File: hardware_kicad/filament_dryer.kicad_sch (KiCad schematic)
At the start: 60 parts, among them J1 grove_vert_holes, J2 USB_C_Receptacle_USB2.0, J3 grove_vert_holes, Q1 NMOS, U1 W25Q128JVS, U2 AMS1117-3.3, U3 RP2040, U4 DS18B20Z, U5 SHT31-DIS, U6 DS18B20Z, X1 12MHz Yangxing Tech X322512MS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

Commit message: Added new parts
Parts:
- removed R11: 10k, Resistor_SMD:R_0402_1005Metric_Pad0.72x0.64mm_HandSolder, symbol 00_project_library:R
- removed TP7: TestPoint, TestPoint:TestPoint_Pad_D1.0mm, symbol Connector:TestPoint
- added C14: 10u, Capacitor_SMD:C_0603_1608Metric, symbol 00_project_library:C
- added HT_FILAMENT_SCL: TestPoint, TestPoint:TestPoint_Pad_D1.5mm, symbol Connector:TestPoint
- added R17, R18: 10k, Resistor_SMD:R_0402_1005Metric_Pad0.72x0.64mm_HandSolder, symbol 00_project_library:R
- added TP6: HT_FILAMENT_SCA, TestPoint:TestPoint_Pad_D1.5mm, symbol Connector:TestPoint
- TP2: value TestPoint -> HT_FILAMENT_GND
- TP3: value TestPoint -> HT_FILAMENT_3V3
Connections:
- net +3V3: now also TP3.1, C14.1, R17.1, R18.1
- net GND: now also TP2.1, U5.2 (ADDR), C14.2
- net HUMIDITY_GROVE_SCL: no longer J1.1
- net HUMIDITY_GROVE_SDA: no longer J1.2
- net HUMIDITY_SCL: no longer R14.2, TP3.1, U5.4 (SCL)
- net HUMIDITY_SDA: no longer R13.2, TP2.1, U5.1 (SDA)
- net TEMP_BOARD_1WIRE: no longer R15.2, TP4.1, U4.4 (DQ)
- net TEMP_GROVE_1WIRE: no longer J3.1, R16.2
- net TEMP_HEATING_1WIRE: no longer R1.2, TP5.1, U6.4 (DQ)
- new net HT_FILAMENT_SCL: HT_FILAMENT_SCL.1, R18.2
- new net HT_FILAMENT_SDA: R17.2, TP6.1
- new net HT_GROVE_SCL: J1.1
- new net HT_GROVE_SDA: J1.2
- new net HT_SILICAGEL_SCL: R14.2, U5.4 (SCL)
- new net HT_SILICAGEL_SDA: R13.2, U5.1 (SDA)
- new net T_BOARD_1WIRE: R15.2, TP4.1, U4.4 (DQ)
- new net T_GROVE_1WIRE: J3.1, R16.2
- new net T_HEATING_1WIRE: R1.2, TP5.1, U6.4 (DQ)
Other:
- note added: "H/T Ambient"
- note added: "H/T Filament"
- note added: "H/T Silicagel"
- note removed: "Humidity"
- moved on the sheet: C13, C15, C20, D2, J1, JP1, Q1, R10, R12, R13, R14, R7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

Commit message: Some more layout
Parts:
- removed JP1: Jumper_2_Bridged, Jumper:SolderJumper-2_P1.3mm_Open_RoundedPad1.0x1.5mm, symbol Jumper:Jumper_2_Bridged
- added D1: HEATER_2, LED_SMD:LED_0603_1608Metric, symbol 00_project_library:LED
- added D4, D5: 1N4148WS, Diode_SMD:D_SOD-323, symbol Diode:1N4148WS
- added D6: FAN_1, LED_SMD:LED_0603_1608Metric, symbol 00_project_library:LED
- added D7: FAN_2, LED_SMD:LED_0603_1608Metric, symbol 00_project_library:LED
- added H5: MountingHole, MountingHole:MountingHole_3.2mm_M3, symbol 00_project_library:MountingHole
- added J4: Peristatic Pump, 00_project_library:grove_vert_holes, symbol 00_project_library:grove_vert_holes
- added Q2, Q3, Q4: NMOS, Package_TO_SOT_SMD:SOT-23, symbol 00_project_library:NMOS
- added R11, R19, R20, R22: 470R, Resistor_SMD:R_0402_1005Metric_Pad0.72x0.64mm_HandSolder, symbol 00_project_library:R
- added R_POWER1_10, R_POWER1_11, R_POWER1_12, R_POWER1_2, R_POWER1_3, R_POWER1_4, R_POWER1_5, R_POWER1_6, R_POWER1_7, R_POWER1_8, R_POWER1_9, R_POWER2_1, R_POWER2_10, R_POWER2_11, R_POWER2_12, R_POWER2_2, R_POWER2_3, R_POWER2_4, R_POWER2_5, R_POWER2_6, R_POWER2_7, R_POWER2_8, R_POWER2_9: 120, Resistor_SMD:R_1206_3216Metric, symbol 00_project_library:R_POWER
- added TP10: FAN_SILICAGEL_BLACK, TestPoint:TestPoint_Pad_D3.0mm, symbol Connector:TestPoint
- added TP7: FAN_AMBIENT_RED, TestPoint:TestPoint_Pad_D3.0mm, symbol Connector:TestPoint
- added TP8: FAN_AMBIENT_BLACK, TestPoint:TestPoint_Pad_D3.0mm, symbol Connector:TestPoint
- added TP9: FAN_SILICAGEL_RED, TestPoint:TestPoint_Pad_D3.0mm, symbol Connector:TestPoint
- D2: value HEATING_LED -> HEATER_1
- H1, H2, H3, H4: footprint MountingHole:MountingHole_2.2mm_M2 -> MountingHole:MountingHole_3.2mm_M3
- J2: renamed from J1; value grove_vert_holes -> H/T Ambient
- J3: value grove_vert_holes -> T Aux
- TP11: renamed from HT_FILAMENT_SCL; value TestPoint -> HT_SILICAGEL_SCL; footprint TestPoint:TestPoint_Pad_D1.5mm -> TestPoint:TestPoint_Pad_D3.0mm
- TP2: value HT_FILAMENT_GND -> HT_SILICAGEL_GND; footprint TestPoint:TestPoint_Pad_D1.5mm -> TestPoint:TestPoint_Pad_D3.0mm
- TP3: value HT_FILAMENT_3V3 -> HT_SILICAGEL_3V3; footprint TestPoint:TestPoint_Pad_D1.5mm -> TestPoint:TestPoint_Pad_D3.0mm
- TP4, TP5: footprint TestPoint:TestPoint_Pad_D2.5mm -> TestPoint:TestPoint_Pad_D1.5mm
- TP6: value HT_FILAMENT_SCA -> HT_SILICAGEL_SCA; footprint TestPoint:TestPoint_Pad_D1.5mm -> TestPoint:TestPoint_Pad_D3.0mm
- U5: value SHT31-DIS -> H/T Filament
- renumbered J2 to J1, R_POWER1 to R_POWER1_1
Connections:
- net HUMIDITY_GROVE_SCL is gone; now on net HT_GROVE_SCL: U3.7 (GPIO5)
- net HUMIDITY_GROVE_SDA is gone; now on net HT_GROVE_SDA: U3.6 (GPIO4)
- net HUMIDITY_SCL is gone; now on net HT_GROVE_SCL: U3.14 (GPIO11)
- net HUMIDITY_SDA is gone; now on net HT_GROVE_SDA: U3.13 (GPIO10)
- net TEMP_BOARD_1WIRE is gone; now on net T_BOARD_1WIRE: U3.2 (GPIO0)
- net TEMP_HEATING_1WIRE is gone; now on net T_HEATING_1WIRE: U3.11 (GPIO8)
- net T_GROVE_1WIRE is gone; now on net T_AUX_1WIRE: J3.1, R16.2
- net +3V3: now also J4.3
- net +5V: now also R_POWER1_1.1, D4.1 (K), D5.1 (K), R_POWER1_10.1, R_POWER1_11.1, R_POWER1_12.1, R_POWER1_2.1, R_POWER1_3.1, R_POWER1_4.1, R_POWER1_5.1, R_POWER1_6.1, R_POWER1_7.1, R_POWER1_8.1, R_POWER1_9.1, R_POWER2_1.1, R_POWER2_10.1, R_POWER2_11.1, R_POWER2_12.1, R_POWER2_2.1, R_POWER2_3.1, R_POWER2_4.1, R_POWER2_5.1, R_POWER2_6.1, R_POWER2_7.1, R_POWER2_8.1, R_POWER2_9.1, TP7.1, TP9.1
- net GND: now also J4.4, Q2.3 (S), Q3.3 (S), Q4.3 (S), R11.2, R19.2, R20.2
- net HT_FILAMENT_SCL: now also R14.2, U3.30 (GPIO19), U5.4 (SCL); no longer R18.2, TP11.1
- net HT_FILAMENT_SDA: now also R13.2, U3.29 (GPIO18), U5.1 (SDA); no longer R17.2, TP6.1
- net HT_SILICAGEL_SCL: now also R18.2, TP11.1; no longer R14.2, U5.4 (SCL)
- net HT_SILICAGEL_SDA: now also R17.2, TP6.1; no longer R13.2, U5.1 (SDA)
- net T_BOARD_1WIRE: now also U3.12 (GPIO9)
- net at Q1.1 (D), R_POWER1_1.2: now also R_POWER1_10.2, R_POWER1_11.2, R_POWER1_12.2, R_POWER1_2.2, R_POWER1_3.2, R_POWER1_4.2, R_POWER1_5.2, R_POWER1_6.2, R_POWER1_7.2, R_POWER1_8.2, R_POWER1_9.2
- net GPIO_HEATER_1: now reaches U3.16 (GPIO13)
- net GPIO_HEATER_1: now also D2.1 (K), Q1.2 (G)
- net GPIO_HEATER_2: now reaches U3.17 (GPIO14)
- net GPIO_HEATER_2: now also D1.1 (K), Q2.2 (G)
- net GPIO_PUMP_STEP: now reaches U3.27 (GPIO16)
- net GPIO_PUMP_STEP: now also R22.1
- removed net GPIO_HEATER: D2.1 (K), Q1.2 (G), U3.12 (GPIO9)
- net TEMP_GROVE_1WIRE renamed T_AUX_1WIRE
- new net: Q2.1 (D), R_POWER2_1.2, R_POWER2_10.2, R_POWER2_11.2, R_POWER2_12.2, R_POWER2_2.2, R_POWER2_3.2, R_POWER2_4.2, R_POWER2_5.2, R_POWER2_6.2, R_POWER2_7.2, R_POWER2_8.2, R_POWER2_9.2
- new net: D1.2 (A), R11.1
- new net: D7.2 (A), R20.1
- new net: D5.2 (A), Q4.1 (D), TP10.1
- new net: D4.2 (A), Q3.1 (D), TP8.1
- new net: D6.2 (A), R19.1
- new net: J4.1, R22.2
- new net GPIO_FAN_AMBIENT: D6.1 (K), Q3.2 (G)
- new net GPIO_FAN_SILICAGEL: D7.1 (K), Q4.2 (G)
- no-connect marks 28 -> 24
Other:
- note added: "Fan Ambient"
- note added: "Fan Silicagel"
- note added: "Heater 1"
- note added: "Heater 2"
- note added: "Mounting Hole"
- note added: "Peristatic Pump"
- note removed: "Heater"
- moved on the sheet: D2, H1, H2, H3, H4, Q1, R7, R_POWER1_1

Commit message: tmp
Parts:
- removed TP4: TestPoint, TestPoint:TestPoint_Pad_D1.5mm, symbol Connector:TestPoint
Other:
- note added: "3D"
- moved on the sheet: H1, H2, H3, H4, H5
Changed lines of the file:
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@@
     (stroke (width 0) (type default))
   )
-  (wire (pts (xy 129.54 260.35) (xy 129.54 256.54))
-    (stroke (width 0) (type default))
-  )
   (wire (pts (xy 50.8 344.17) (xy 50.8 350.52))
     (stroke (width 0) (type default))
@@
     (fill (type none))
   )
-  (rectangle (start 24.13 247.65) (end 49.53 284.48)
+  (rectangle (start 63.5 478.79) (end 88.9 515.62)
+    (stroke (width 0) (type default))
+    (fill (type none))
+  )
+  (rectangle (start 31.75 478.79) (end 57.15 515.62)
     (stroke (width 0) (type default))
     (fill (type none))
@@
     (effects (font (size 1.27 1.27) (thickness 0.254) bold) (justify left bottom))
   )
-  (text "Mounting Hole" (at 29.21 252.73 0)
+  (text "Mounting Hole" (at 36.83 483.87 0)
     (effects (font (size 1.27 1.27) (thickness 0.254) bold) (justify left bottom))
   )
@@
     (effects (font (size 1.27 1.27) (thickness 0.254) bold) (justify left bottom))
   )
+  (text "3D" (at 66.04 483.87 0)
+    (effects (font (size 1.27 1.27) (thickness 0.254) bold) (justify left bottom))
+  )
   (text "Make sure 27R are close to RP2040" (at 132.08 130.175 90)
     (effects (font (size 1.27 1.27)) (justify left bottom))
@@
     )
   )
-  (symbol (lib_id "00_project_library:MountingHole") (at 30.48 278.13 0) (unit 1)
+  (symbol (lib_id "00_project_library:MountingHole") (at 38.1 509.27 0) (unit 1)
     (in_bom yes) (on_board yes) (dnp no)
-    (property "Reference" "H5" (at 33.02 276.9616 0)
+    (property "Reference" "H5" (at 40.64 508.1016 0)
       (effects (font (size 0.8 0.8)) (justify left))
     )
-    (property "Value" "MountingHole" (at 33.02 279.273 0)
+    (property "Value" "MountingHole" (at 40.64 510.413 0)
       (effects (font (size 0.8 0.8)) (justify left))
     )
-    (property "Footprint" "MountingHole:MountingHole_3.2mm_M3" (at 30.48 278.13 0)
+    (property "Footprint" "MountingHole:MountingHole_3.2mm_M3" (at 38.1 509.27 0)
       (effects (font (size 0.8 0.8)) hide)
     )
-    (property "Datasheet" "~" (at 30.48 278.13 0)
+    (property "Datasheet" "~" (at 38.1 509.27 0)
       (effects (font (size 0.8 0.8)) hide)
     )
@@
     )
   )
-  (symbol (lib_id "Connector:TestPoint") (at 129.54 260.35 180) (unit 1)
-    (in_bom yes) (on_board yes) (dnp no)
-    (property "Reference" "TP4" (at 130.81 266.7 0)
-      (effects (font (size 1.27 1.27)) (justify left))
-    )
-    (property "Value" "TestPoint" (at 133.35 269.24 0)
-      (effects (font (size 1.27 1.27)) (justify left))
-    )
-    (property "Footprint" "TestPoint:TestPoint_Pad_D1.5mm" (at 124.46 260.35 0)
-      (effects (font (size 1.27 1.27)) hide)
-    )
-    (property "Datasheet" "~" (at 124.46 260.35 0)
-      (effects (font (size 1.27 1.27)) hide)
-    )
-    (pin "1")
-    (instances
-      (project "filament_dryer"
-        (path "/35c47459-45a7-4753-acae-c8b47e7575e1"
-          (reference "TP4") (unit 1)
-        )
-      )
-    )
-  )
   (symbol (lib_id "power:GND") (at 36.83 209.55 0) (unit 1)
     (in_bom yes) (on_board yes) (dnp no)
@@
     )
   )
-  (symbol (lib_id "00_project_library:MountingHole") (at 30.48 267.97 0) (unit 1)
+  (symbol (lib_id "00_project_library:MountingHole") (at 38.1 499.11 0) (unit 1)
     (in_bom yes) (on_board yes) (dnp no)
-    (property "Reference" "H3" (at 33.02 266.8016 0)
+    (property "Reference" "H3" (at 40.64 497.9416 0)
       (effects (font (size 0.8 0.8)) (justify left))
     )
-    (property "Value" "MountingHole" (at 33.02 269.113 0)
+    (property "Value" "MountingHole" (at 40.64 500.253 0)
       (effects (font (size 0.8 0.8)) (justify left))
     )
-    (property "Footprint" "MountingHole:MountingHole_3.2mm_M3" (at 30.48 267.97 0)
+    (property "Footprint" "MountingHole:MountingHole_3.2mm_M3" (at 38.1 499.11 0)
       (effects (font (size 0.8 0.8)) hide)
     )
-    (property "Datasheet" "~" (at 30.48 267.97 0)
+    (property "Datasheet" "~" (at 38.1 499.11 0)
       (effects (font (size 0.8 0.8)) hide)
     )
@@
     )
   )
-  (symbol (lib_id "00_project_library:MountingHole") (at 30.48 257.81 0) (unit 1)
+  (symbol (lib_id "00_project_library:MountingHole") (at 38.1 488.95 0) (unit 1)
     (in_bom yes) (on_board yes) (dnp no)
-    (property "Reference" "H1" (at 33.02 256.6416 0)
+    (property "Reference" "H1" (at 40.64 487.7816 0)
       (effects (font (size 0.8 0.8)) (justify left))
     )
-    (property "Value" "MountingHole" (at 33.02 258.953 0)
+    (property "Value" "MountingHole" (at 40.64 490.093 0)
       (effects (font (size 0.8 0.8)) (justify left))
     )
-    (property "Footprint" "MountingHole:MountingHole_3.2mm_M3" (at 30.48 257.81 0)
+    (property "Footprint" "MountingHole:MountingHole_3.2mm_M3" (at 38.1 488.95 0)
       (effects (font (size 0.8 0.8)) hide)
     )
-    (property "Datasheet" "~" (at 30.48 257.81 0)
+    (property "Datasheet" "~" (at 38.1 488.95 0)
       (effects (font (size 0.8 0.8)) hide)
     )
@@
     )
   )
-  (symbol (lib_id "00_project_library:MountingHole") (at 30.48 273.05 0) (unit 1)
+  (symbol (lib_id "00_project_library:MountingHole") (at 38.1 504.19 0) (unit 1)
     (in_bom yes) (on_board yes) (dnp no)
-    (property "Reference" "H4" (at 33.02 271.8816 0)
+    (property "Reference" "H4" (at 40.64 503.0216 0)
       (effects (font (size 0.8 0.8)) (justify left))
     )
-    (property "Value" "MountingHole" (at 33.02 274.193 0)
+    (property "Value" "MountingHole" (at 40.64 505.333 0)
       (effects (font (size 0.8 0.8)) (justify left))
     )
-    (property "Footprint" "MountingHole:MountingHole_3.2mm_M3" (at 30.48 273.05 0)
+    (property "Footprint" "MountingHole:MountingHole_3.2mm_M3" (at 38.1 504.19 0)
       (effects (font (size 0.8 0.8)) hide)
     )
-    (property "Datasheet" "~" (at 30.48 273.05 0)
+    (property "Datasheet" "~" (at 38.1 504.19 0)
       (effects (font (size 0.8 0.8)) hide)
     )
@@
     )
   )
-  (symbol (lib_id "00_project_library:MountingHole") (at 30.48 262.89 0) (unit 1)
+  (symbol (lib_id "00_project_library:MountingHole") (at 38.1 494.03 0) (unit 1)
     (in_bom yes) (on_board yes) (dnp no)
-    (property "Reference" "H2" (at 33.02 261.7216 0)
+    (property "Reference" "H2" (at 40.64 492.8616 0)
       (effects (font (size 0.8 0.8)) (justify left))
     )
-    (property "Value" "MountingHole" (at 33.02 264.033 0)
+    (property "Value" "MountingHole" (at 40.64 495.173 0)
       (effects (font (size 0.8 0.8)) (justify left))
     )
-    (property "Footprint" "MountingHole:MountingHole_3.2mm_M3" (at 30.48 262.89 0)
+    (property "Footprint" "MountingHole:MountingHole_3.2mm_M3" (at 38.1 494.03 0)
       (effects (font (size 0.8 0.8)) hide)
     )
-    (property "Datasheet" "~" (at 30.48 262.89 0)
+    (property "Datasheet" "~" (at 38.1 494.03 0)
       (effects (font (size 0.8 0.8)) hide)
     )

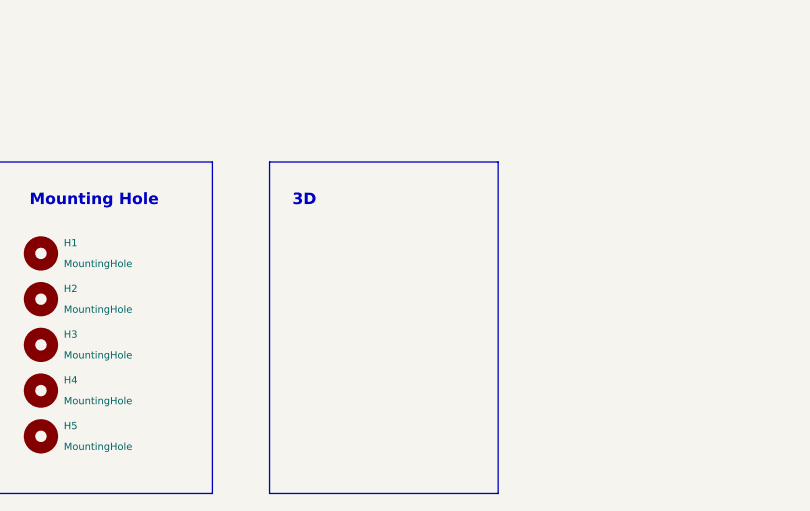
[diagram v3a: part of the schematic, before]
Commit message: Update 3d footprint
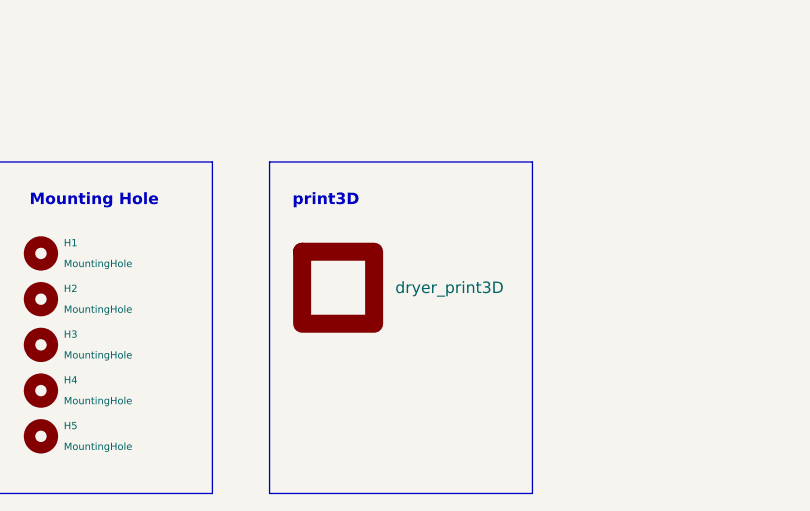
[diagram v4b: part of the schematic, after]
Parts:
- added dryer_print3D1: dryer_print3D, 00_project_library:dryer_print3d, symbol 00_project_library:dryer_print3d
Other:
- note added: "print3D"
- note removed: "3D"
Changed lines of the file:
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@@
     (fill (type none))
   )
-  (rectangle (start 63.5 478.79) (end 88.9 515.62)
+  (rectangle (start 63.5 478.79) (end 92.71 515.62)
     (stroke (width 0) (type default))
     (fill (type none))
@@
     (effects (font (size 1.27 1.27) (thickness 0.254) bold) (justify left bottom))
   )
-  (text "3D" (at 66.04 483.87 0)
+  (text "print3D" (at 66.04 483.87 0)
     (effects (font (size 1.27 1.27) (thickness 0.254) bold) (justify left bottom))
   )
@@
         )
       )
+    )
+  )
+  (symbol (lib_id "00_project_library:dryer_print3d") (at 71.12 492.76 0) (unit 1)
+    (in_bom no) (on_board yes) (dnp no) (fields_autoplaced)
+    (property "Reference" "dryer_print3D1" (at 71.12 499.11 0)
+      (effects (font (size 1.27 1.27)) hide)
+    )
+    (property "Value" "dryer_print3D" (at 77.47 492.76 0)
+      (effects (font (size 1.27 1.27)) (justify left))
+    )
+    (property "Footprint" "00_project_library:dryer_print3d" (at 69.85 501.65 0)
+      (effects (font (size 1.27 1.27)) hide)
+    )
+    (property "Datasheet" "" (at 71.12 492.76 0)
+      (effects (font (size 1.27 1.27)) hide)
+    )
+    (instances
+      (project "filament_dryer"
+        (path "/35c47459-45a7-4753-acae-c8b47e7575e1"
+          (reference "dryer_print3D1") (unit 1)
+        )
+      )

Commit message: routing
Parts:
- removed R1: 4k7, Resistor_SMD:R_0402_1005Metric_Pad0.72x0.64mm_HandSolder, symbol 00_project_library:R
- removed R17, R18: 10k, Resistor_SMD:R_0402_1005Metric_Pad0.72x0.64mm_HandSolder, symbol 00_project_library:R
- removed TP5: TestPoint, TestPoint:TestPoint_Pad_D1.5mm, symbol Connector:TestPoint
- removed U6: DS18B20Z, Package_SO:SOIC-8_3.9x4.9mm_P1.27mm, symbol 00_project_library:DS18B20Z
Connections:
- net HT_SILICAGEL_SCL is gone; now on net HT_BOARD_SCL: TP11.1
- net HT_SILICAGEL_SDA is gone; now on net HT_BOARD_SDA: TP6.1
- net +3V3: now also U5.2 (ADDR)
- net GND: no longer U5.2 (ADDR)
- net GPIO_FAN_AMBIENT: now also U3.32 (GPIO21)
- net T_BOARD_1WIRE: no longer R15.2, U4.4 (DQ)
- net T_HEATING_1WIRE: now also R15.2, U3.18 (GPIO15), U4.4 (DQ); no longer U3.11 (GPIO8)
- net HT_BOARD_SDA: now reaches U3.38 (GPIO26/ADC0)
- net HT_BOARD_SDA: now also R13.2, U5.1 (SDA)
- net HT_BOARD_SCL: now reaches U3.39 (GPIO27/ADC1)
- net HT_BOARD_SCL: now also R14.2, U5.4 (SCL)
- removed net HT_FILAMENT_SCL: R14.2, U3.30 (GPIO19), U5.4 (SCL)
- removed net HT_FILAMENT_SDA: R13.2, U3.29 (GPIO18), U5.1 (SDA)
- no-connect marks 24 -> 21
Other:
- note added: "H/T Ambient I2C0 0x44"
- note added: "H/T Filament I2C1 0x45"
- note added: "H/T Silicagel I2C1 0x44"
- note removed: "H/T Ambient"
- note removed: "H/T Filament"
- note removed: "H/T Silicagel"
- moved on the sheet: C14, C20, J3, J4, R12, R16, R22

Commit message: 2023-08-20 review schematics
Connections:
- net T_AUX_1WIRE: now also U3.15 (GPIO12); no longer U3.4 (GPIO2)
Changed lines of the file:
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@@
   (no_connect (at 48.26 106.68))
   (no_connect (at 273.05 250.19))
-  (no_connect (at 48.26 78.74))
+  (no_connect (at 48.26 50.8))
   (no_connect (at 119.38 96.52))
   (no_connect (at 48.26 63.5))
@@
     (stroke (width 0) (type default))
   )
-  (wire (pts (xy 44.45 50.8) (xy 48.26 50.8))
+  (wire (pts (xy 40.64 78.74) (xy 48.26 78.74))
     (stroke (width 0) (type default))
   )
@@
     (effects (font (size 1.27 1.27) italic) (justify right bottom))
   )
-  (label "T_AUX_1WIRE" (at 44.45 50.8 180) (fields_autoplaced)
+  (label "T_AUX_1WIRE" (at 40.64 78.74 180) (fields_autoplaced)
     (effects (font (size 1.27 1.27)) (justify right bottom))
   )

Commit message: Removed resistors, add locked zones
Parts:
- J4: value Peristatic Pump -> Peristaltic Pump
- TP10: value FAN_SILICAGEL_BLACK -> FAN_SILICAGEL_GND
- TP7: value FAN_AMBIENT_RED -> FAN_AMBIENT_5V
- TP8: value FAN_AMBIENT_BLACK -> FAN_AMBIENT_GND
- TP9: value FAN_SILICAGEL_RED -> FAN_SILICAGEL_5V
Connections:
- net +5V: now also D1.2 (A), D2.2 (A)
- net GND: no longer R11.2, R7.2
- net GPIO_FAN_AMBIENT: now also D6.2 (A); no longer D6.1 (K)
- net GPIO_FAN_SILICAGEL: now also D7.2 (A); no longer D7.1 (K)
- net GPIO_HEATER_1: no longer D2.1 (K)
- net GPIO_HEATER_2: no longer D1.1 (K)
- net at Q1.1 (D), R_POWER1_1.2, R_POWER1_10.2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: now also R7.2
- net at Q2.1 (D), R_POWER2_1.2, R_POWER2_10.2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: now also R11.2
- net at R11.1: now also D1.1 (K); no longer D1.2 (A)
- net at R20.1: now also D7.1 (K); no longer D7.2 (A)
- net at R19.1: now also D6.1 (K); no longer D6.2 (A)
- net at R7.1: now also D2.1 (K); no longer D2.2 (A)
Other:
- note added: "Peristaltic Pump"
- note removed: "Peristatic Pump"
- moved on the sheet: D1, D2, D6, D7, Q1, R11, R7
